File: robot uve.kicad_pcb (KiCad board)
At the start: 2 copper layers, 100 x 100 mm, 63 parts, among them J1 pulsador1, J10 HC-SR04, J11 HC-SR04, J12 HC-SR04, J13 NC - C - NA, J14 I2C_B, J15 I2C_C, J16 NeoPixel, J17 neopixel, J18 +5V IN, J19 GND, J2 I2C_A, J20 pulsador2, J21 IR, J22 RST, J3 NC - C - NA, J4 comunicacion a rpi, J5 12V IN, J6 GND, J7 HC-SR04, J8 HC-SR04, J9 HC-SR04, K1 RELAY_C, K3 RELAY_C, P1 Digital, P10 CONN_01X01, P11 CONN_01X01, P12 CONN_01X01, P13 CONN_01X01, P14 motor3, P15 motor2, P16 Sensores de Linea, P17 motor1, P18 motor4, P2 Power, P3 Analog, P4 Analog, P5 PWM, P6 PWM, P7 Communication, P8 CONN_01X01, P9 CONN_01X01, Q1 2N7002, Q3 2N7002, Q4 2N7002, SW1 SW_PUSH

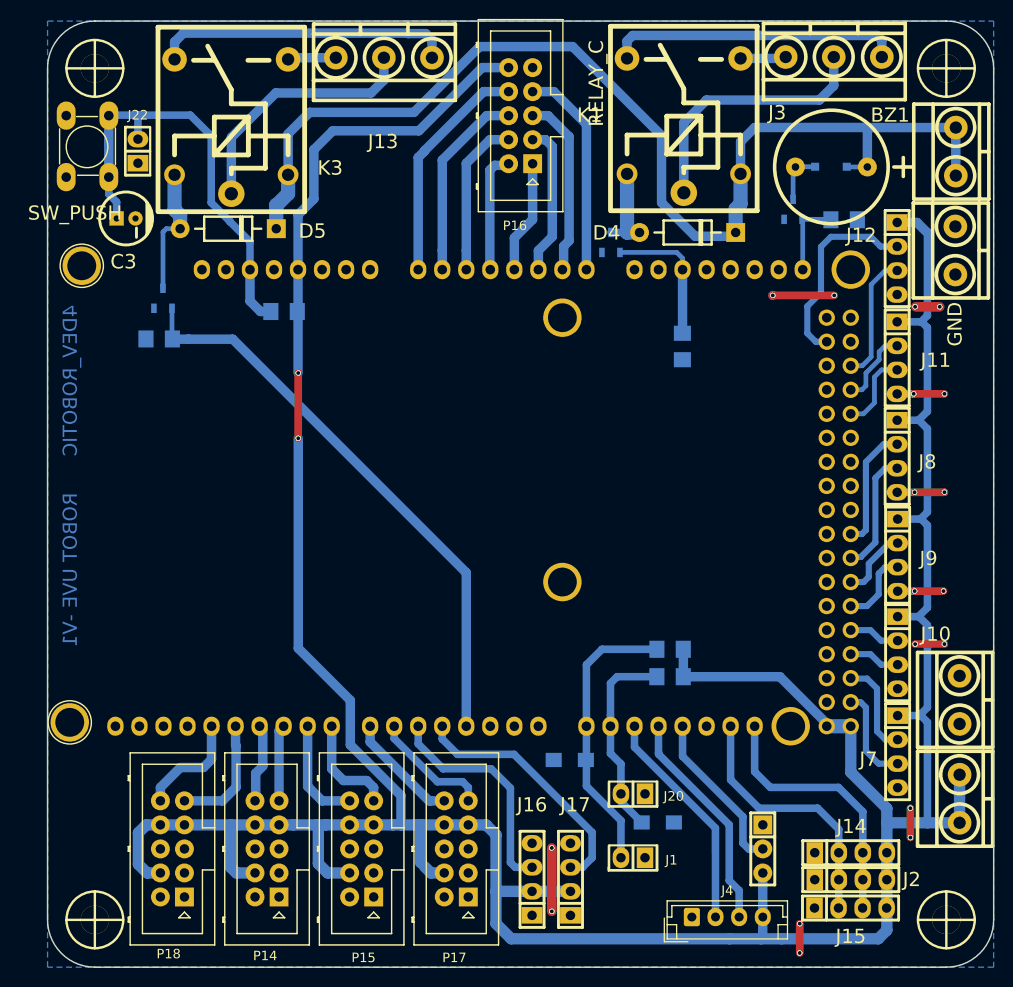
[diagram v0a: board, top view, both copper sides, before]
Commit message: Alineación de vias
Acomode las vias de GND del lateral derecho y genere el archivo para la fabricacion casera.
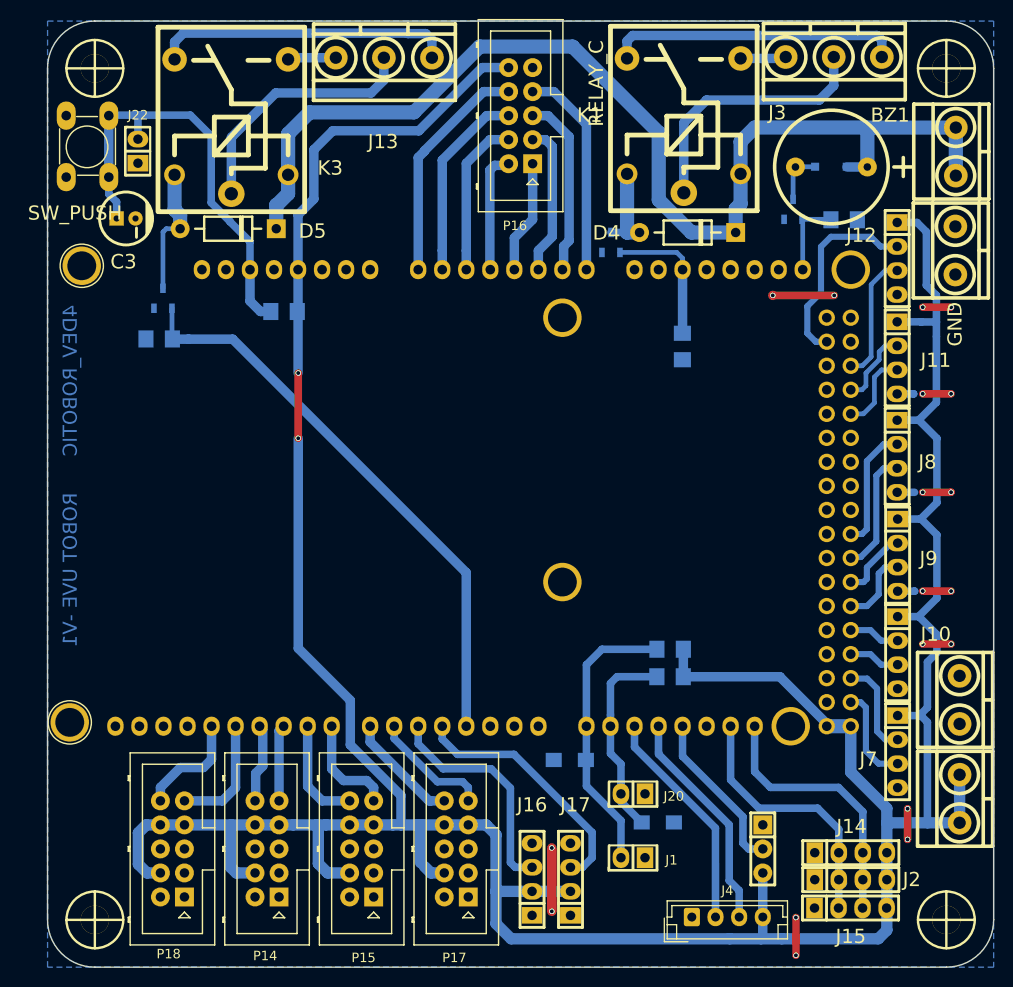
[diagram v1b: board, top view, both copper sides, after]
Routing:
- net +5V: track 378.1 -> 382.4 mm
- net GND: track 39.9 -> 40.8 mm
- net /12V: track 118.9 -> 118.3 mm
